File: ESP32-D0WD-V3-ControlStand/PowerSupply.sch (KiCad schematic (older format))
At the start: 5 parts

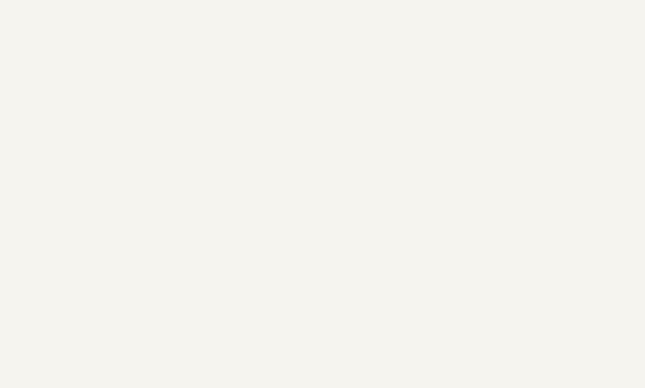
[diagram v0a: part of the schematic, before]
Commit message: Nearly complete schematic.  Added Antenna footprint.
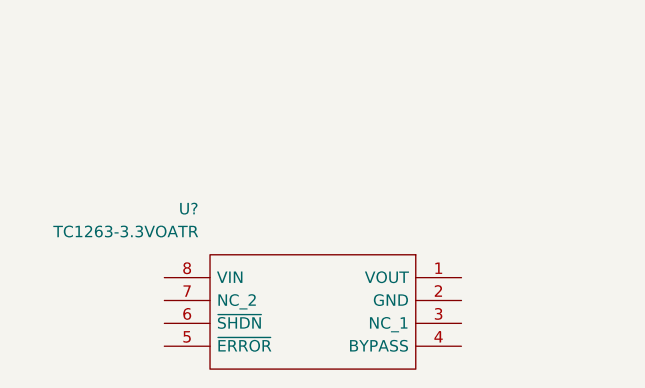
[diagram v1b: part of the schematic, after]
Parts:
- added U?: TC1263-3.3VOATR, Housings_SOIC:SO-8_5.3x6.2mm_Pitch1.27mm, symbol TC1263-3.3VOATR
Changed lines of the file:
@@
 $Descr E 44000 34000
 encoding utf-8
-Sheet 5 6
+Sheet 5 7
 Title "ESP32-D0WD-V3-ControlStand"
 Date "2022-07-25"
@@
 	1    0    0    -1
 $EndComp
+$Comp
+L TC1263-3.3VOATR U?
+U 1 1 62E1190F
+P 5500 4800
+F 0 "U?" H 6650 5100 50  0000 L CNN
+F 1 "TC1263-3.3VOATR" H 6650 5000 50  0000 L CNN
+F 2 "Housings_SOIC:SO-8_5.3x6.2mm_Pitch1.27mm" H 6650 4900 50  0001 L CNN
+F 3 "http://ww1.microchip.com/downloads/en/DeviceDoc/21374D.pdf" H 6650 4800 50  0001 L CNN
+F 4 "LDO Voltage Regulators 500mA Fixed Out Adj" H 6650 4700 50  0001 L CNN "Description"
+F 5 "1.75" H 6650 4600 50  0001 L CNN "Height"
+F 6 "Microchip" H 6650 4300 50  0001 L CNN "Manufacturer_Name"
+F 7 "TC1263-3.3VOATR" H 6650 4200 50  0001 L CNN "Manufacturer_Part_Number"
+	1    5500 4800
+	-1   0    0    -1
+$EndComp
 Wire Wire Line

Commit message: Complete PS, work on parts spec.
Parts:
- added C?: 10uf, Capacitors_SMD:CP_Elec_4x5.7, symbol CP1_Small
- added C? (x2): 4.7uf, Capacitors_SMD:CP_Elec_4x5.7, symbol CP1_Small
- added C?: .1uf, symbol C_Small
- added C?: 1uf, symbol CP1_Small
- added C?: 470pf, symbol C_Small
- added D? (x2): DFLS240-7, Diodes_SMD:D_PowerDI-123, symbol D_Schottky
- added D?: DFLS240-7, Diodes_SMD:D_PowerDI-12, symbol D_Schottky
- added D? (x3): LED, LEDs:LED_0402, symbol LED
- added D?: SMAJ5.0A/TR13, Diodes_SMD:D_SMA, symbol D_Zener_Small_ALT
- added J?: Barrel_Jack, Connectors:BARREL_JACK, symbol Barrel_Jack
- added J?: Battery, Connectors_JST:JST_PH_S2B-PH-SM4-TB_02x2.00mm_Angled, symbol Conn_01x02
- added R?: 330K, Resistors_SMD:R_0402, symbol R
- added R?: 110K, Resistors_SMD:R_0402, symbol R
- added R? (x3): 470, Resistors_SMD:R_0402, symbol R
- added R? (x2): 10K, Resistors_SMD:R_0402, symbol R
- added R?: 2K, Resistors_SMD:R_0402, symbol R
- added R?: 5K, Resistors_SMD:R_0402, symbol R
- added SW?: On/Off, Buttons_Switches_SMD:SW_SPDT_CK-JS102011SAQN, symbol SW_SPDT
- added U?: MCP73871, Housings_DFN_QFN:QFN-20-1EP_4x4mm_Pitch0.5mm, symbol MCP73871
- C?: footprint ~ -> Capacitors_SMD:CP_Elec_8x10; Mouser Part Number 140-REA220M2ABK0811P -> 647-UUX2A220MNL6GS
- C?: footprint ~ -> Capacitors_SMD:CP_Elec_8x10; Mouser Part Number 140-REA221M1EBK0811P -> 647-UWT1E221MNL1GS
- D?: footprint ~ -> Diodes_SMD:D_SMB; Mouser Part Number 625-SB160-E3 -> 610-CMSH1-60TR13
- L?: footprint ~ -> SRN1060:SRN1060; Mouser Part Number PE-52627NL -> 652-SRN1060-331M
- U?: value LM2574N-5.0 -> LM2574HVM-5.0; footprint ~ -> SOIC_Wide:SOIC-14_7.4x8.7mm_Pitch1.27mm; symbol LM2574N-5.0 -> LM2574HVM-5.0; Mouser Part Number 926-LM2574N-5.0/NOPB -> 926-LM2574HVM5.0NOPB
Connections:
- net +12V: now also U?.10 (Vin); no longer U?.5 (Vin)
- net +5V: now also U?.3 (FB), D?.2 (A); no longer U?.1 (FB)
- net GND: now also U?.2 (GND), U?.5 (Oh/Off), U?.6 (PwrGnd), C?.1, C?.2, C?.2, C?.2, C?.2, C?.2, D?.2 (A), J?.2, J?.2 (Pin_2), R?.2, R?.2, R?.2, R?.2, U?.10 (GND), U?.11 (GND), U?.21 (GND); no longer U?.2 (SigGnd), U?.3 (Oh/Off)
- net at D?.2 (K), L?.2: now also U?.12 (Out); no longer U?.7 (Out)
- net +3V3: now reaches U?.1 (VOUT)
- net +3V3: now also C?.1
- net at U?.4 (BYPASS): now also C?.1
- net at U?.6 (~SHDN): now also U?.8 (VIN), C?.2, D?.1 (K), D?.1 (K), SW?.2 (B)
- new net: C?.1, D?.1 (K), D?.2 (A), D?.2 (A), D?.2 (A), J?.1, R?.2, R?.2, U?.18 (IN), U?.19 (IN)
- new net: C?.1, J?.1 (Pin_1), U?.14 (BAT+), U?.15 (BAT+), U?.16 (BAT+)
- new net: C?.1, D?.2 (A), U?.1 (OUT), U?.20 (OUT)
- new net: R?.1, U?.12 (PROG3)
- new net: R?.1, U?.13 (PROG1)
- new net: R?.1, U?.17 (CE), U?.3 (SEL), U?.4 (PROG2), U?.9 (~TE)
- new net: R?.1, R?.1, U?.2 (VPCC)
- new net: R?.1, U?.5 (THERM)
- new net: R?.1, U?.6 (~PG)
- new net: R?.1, U?.7 (STAT2)
- new net: R?.1, U?.8 (STAT1/~LBO)
- new net: D?.1 (K), R?.2 (x3)
- new net: D?.1 (K), SW?.1 (A)
- new net VBUS: D?.2 (A)
- no-connect marks 0 -> 4
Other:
- moved on the sheet: U?

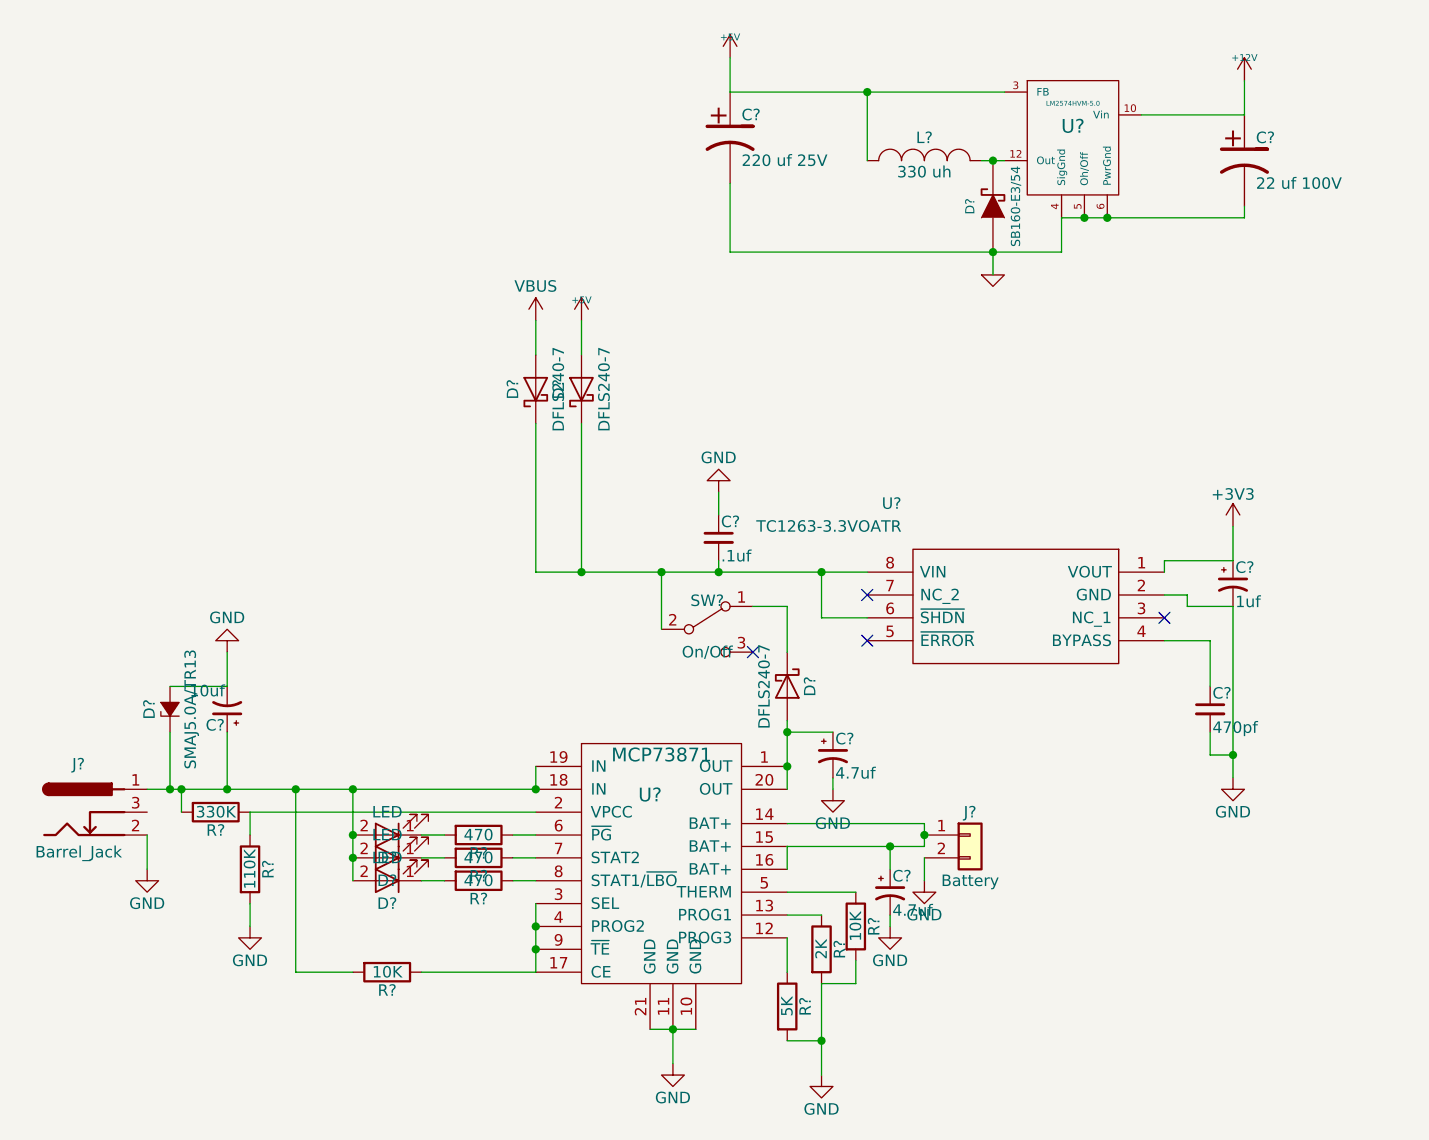
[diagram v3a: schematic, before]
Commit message: Completed parts spec for ESP32-D0WD-V3-ControlStand.
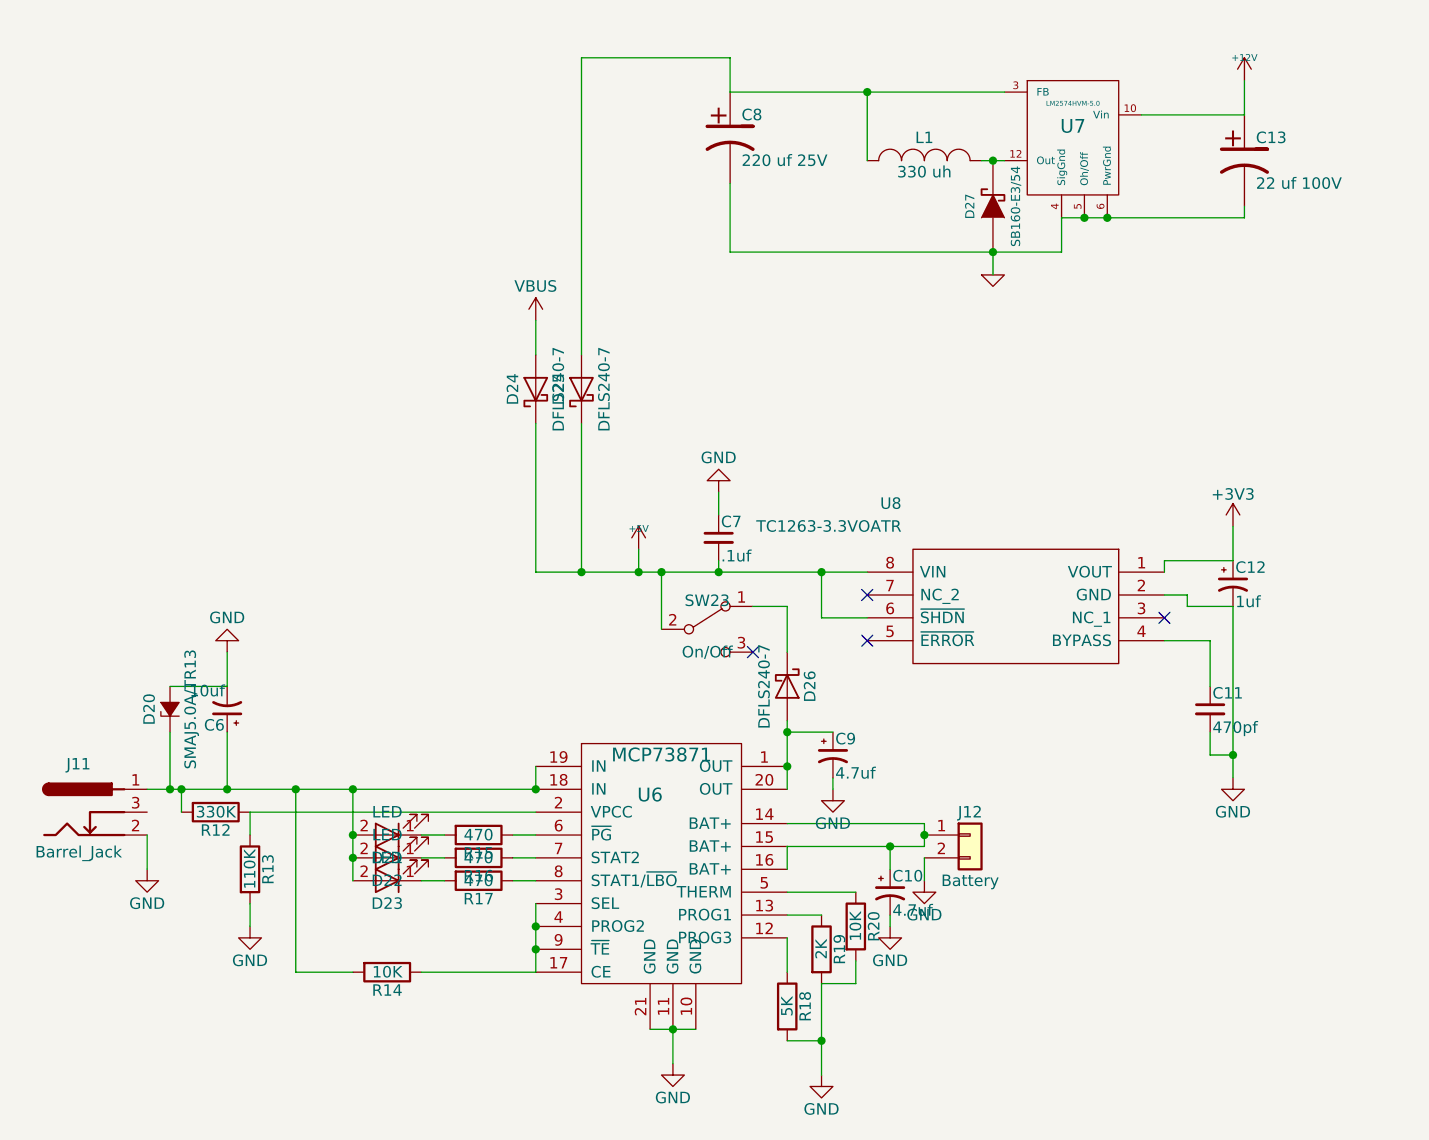
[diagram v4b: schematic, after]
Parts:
- C11: renamed from C?; footprint (none) -> Capacitors_SMD:C_0402; Mouser Part Number (none) -> 80-C0402C471K4RAUTO
- C12: renamed from C?; footprint (none) -> MyCaps:C_0603_POL; Mouser Part Number (none) -> 74-TMCJ1C105MTRF
- C7: renamed from C?; footprint (none) -> Capacitors_SMD:C_0402; Mouser Part Number (none) -> 81-GRM155R62A104KE4J
- gave numbers to parts that had none: 29
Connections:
- net +5V: now also C7.2, D24.1 (K), D25.1 (K), SW23.2 (B), U8.6 (~SHDN), U8.8 (VIN); no longer C8.1, D25.2 (A), L1.1, U7.3 (FB)
- new net: C8.1, D25.2 (A), L1.1, U7.3 (FB)

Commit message: Working on the PCB Layout.
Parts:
- D25: footprint Diodes_SMD:D_PowerDI-12 -> Diodes_SMD:D_PowerDI-123
- J12: footprint Connectors_JST:JST_PH_S2B-PH-SM4-TB_02x2.00mm_Angled -> Connectors_JST:JST_PH_B2B-PH-SM4-TB_02x2.00mm_Straight; Manufacturer_Part_Number (none) -> B2B-PH-SM4-TB; Manufaturer_Name (none) -> JST
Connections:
- net +3V3 renamed +3.3V
- no-connect marks 4 -> 13
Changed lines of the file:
@@
 LIBS:mcp73871
 LIBS:lm2574n-5
+LIBS:mechanical
+LIBS:graphic_symbols
 LIBS:ESP32-D0WD-V3-ControlStand-cache
 EELAYER 25 0
@@
 $EndComp
 $Comp
-L GND-RESCUE-ESP32ControlStand #PWR56
+L GND-RESCUE-ESP32ControlStand #PWR045
 U 1 1 62DF1557
 P 4850 3400
-F 0 "#PWR56" H 4850 3400 30  0001 C CNN
+F 0 "#PWR045" H 4850 3400 30  0001 C CNN
 F 1 "GND" H 4850 3330 30  0001 C CNN
 F 2 "" H 4850 3400 60  0000 C CNN
@@
 $EndComp
 $Comp
-L +12V #PWR59
+L +12V #PWR046
 U 1 1 62DF1558
 P 5950 2550
-F 0 "#PWR59" H 5950 2500 20  0001 C CNN
+F 0 "#PWR046" H 5950 2500 20  0001 C CNN
 F 1 "+12V" H 5950 2650 30  0000 C CNN
 F 2 "" H 5950 2550 60  0000 C CNN
@@
 $EndComp
 $Comp
-L VBUS #PWR48
+L VBUS #PWR047
 U 1 1 62E2AE4F
 P 2850 3600
-F 0 "#PWR48" H 2850 3450 50  0001 C CNN
+F 0 "#PWR047" H 2850 3450 50  0001 C CNN
 F 1 "VBUS" H 2850 3750 50  0000 C CNN
 F 2 "" H 2850 3600 50  0001 C CNN
@@
 $EndComp
 $Comp
-L +5V #PWR49
+L +5V #PWR048
 U 1 1 62E2AF43
 P 3300 4600
-F 0 "#PWR49" H 3300 4690 20  0001 C CNN
+F 0 "#PWR048" H 3300 4690 20  0001 C CNN
 F 1 "+5V" H 3300 4690 30  0000 C CNN
 F 2 "" H 3300 4600 60  0000 C CNN
@@
 $EndComp
 $Comp
-L GND #PWR45
+L GND #PWR049
 U 1 1 62E2B93A
 P 1150 6000
-F 0 "#PWR45" H 1150 5750 50  0001 C CNN
+F 0 "#PWR049" H 1150 5750 50  0001 C CNN
 F 1 "GND" H 1150 5850 50  0000 C CNN
 F 2 "" H 1150 6000 50  0001 C CNN
@@
 F 0 "D25" H 3050 4000 50  0000 C CNN
 F 1 "DFLS240-7" H 3050 3800 50  0000 C CNN
-F 2 "Diodes_SMD:D_PowerDI-12" H 3050 3900 50  0001 C CNN
+F 2 "Diodes_SMD:D_PowerDI-123" H 3050 3900 50  0001 C CNN
 F 3 "" H 3050 3900 50  0001 C CNN
 F 4 "621-DFLS240-7" H 3050 3900 60  0001 C CNN "Mouser Part Number"
@@
 F 0 "J12" H 4750 5950 50  0000 C CNN
 F 1 "Battery" H 4750 5650 50  0000 C CNN
-F 2 "Connectors_JST:JST_PH_S2B-PH-SM4-TB_02x2.00mm_Angled" H 4750 5850 50  0001 C CNN
+F 2 "Connectors_JST:JST_PH_B2B-PH-SM4-TB_02x2.00mm_Straight" H 4750 5850 50  0001 C CNN
 F 3 "" H 4750 5850 50  0001 C CNN
+F 4 "JST" H 4750 5850 60  0001 C CNN "Manufaturer_Name"
+F 5 "B2B-PH-SM4-TB" H 4750 5850 60  0001 C CNN "Manufacturer_Part_Number"
 	1    4750 5850
 	1    0    0    -1
 $EndComp
 $Comp
-L GND #PWR55
+L GND #PWR050
 U 1 1 62E2DC33
 P 4550 6050
-F 0 "#PWR55" H 4550 5800 50  0001 C CNN
+F 0 "#PWR050" H 4550 5800 50  0001 C CNN
 F 1 "GND" H 4550 5900 50  0000 C CNN
 F 2 "" H 4550 6050 50  0001 C CNN
@@
 Connection ~ 3450 6700
 $Comp
-L GND #PWR50
+L GND #PWR051
 U 1 1 62E30901
 P 3450 6850
-F 0 "#PWR50" H 3450 6600 50  0001 C CNN
+F 0 "#PWR051" H 3450 6600 50  0001 C CNN
 F 1 "GND" H 3450 6700 50  0000 C CNN
 F 2 "" H 3450 6850 50  0001 C CNN
@@
 	1600 5750 1600 5850
 $Comp
-L GND #PWR47
+L GND #PWR052
 U 1 1 62E319CD
 P 1600 6250
-F 0 "#PWR47" H 1600 6000 50  0001 C CNN
+F 0 "#PWR052" H 1600 6000 50  0001 C CNN
 F 1 "GND" H 1600 6100 50  0000 C CNN
 F 2 "" H 1600 6250 50  0001 C CNN
@@
 	1250 5200 1500 5200
 $Comp
-L GND #PWR46
+L GND #PWR053
 U 1 1 62E3313D
 P 1500 5050
-F 0 "#PWR46" H 1500 4800 50  0001 C CNN
+F 0 "#PWR053" H 1500 4800 50  0001 C CNN
 F 1 "GND" H 1500 4900 50  0000 C CNN
 F 2 "" H 1500 5050 50  0001 C CNN
@@
 Connection ~ 3950 5400
 $Comp
-L GND #PWR53
+L GND #PWR054
 U 1 1 62E341D5
 P 4150 5650
-F 0 "#PWR53" H 4150 5400 50  0001 C CNN
+F 0 "#PWR054" H 4150 5400 50  0001 C CNN
 F 1 "GND" H 4150 5500 50  0000 C CNN
 F 2 "" H 4150 5650 50  0001 C CNN
@@
 	4150 5600 4150 5650
 $Comp
-L GND #PWR54
+L GND #PWR055
 U 1 1 62E342FA
 P 4400 6250
-F 0 "#PWR54" H 4400 6000 50  0001 C CNN
+F 0 "#PWR055" H 4400 6000 50  0001 C CNN
 F 1 "GND" H 4400 6100 50  0000 C CNN
 F 2 "" H 4400 6250 50  0001 C CNN
@@
 	4250 6500 4250 6400
 $Comp
-L GND #PWR52
+L GND #PWR056
 U 1 1 62E35319
 P 4100 6900
-F 0 "#PWR52" H 4100 6650 50  0001 C CNN
+F 0 "#PWR056" H 4100 6650 50  0001 C CNN
 F 1 "GND" H 4100 6750 50  0000 C CNN
 F 2 "" H 4100 6900 50  0001 C CNN
@@
 Connection ~ 3650 4700
 $Comp
-L GND #PWR51
+L GND #PWR057
 U 1 1 62E36914
 P 3650 4350
-F 0 "#PWR51" H 3650 4100 50  0001 C CNN
+F 0 "#PWR057" H 3650 4100 50  0001 C CNN
 F 1 "GND" H 3650 4200 50  0000 C CNN
 F 2 "" H 3650 4350 50  0001 C CNN
@@
 	5800 5500 5800 5400
 $Comp
-L GND #PWR58
+L GND #PWR058
 U 1 1 62E37013
 P 5900 5600
-F 0 "#PWR58" H 5900 5350 50  0001 C CNN
+F 0 "#PWR058" H 5900 5350 50  0001 C CNN
 F 1 "GND" H 5900 5450 50  0000 C CNN
 F 2 "" H 5900 5600 50  0001 C CNN
@@
 Connection ~ 5900 5500
 $Comp
-L +3V3 #PWR57
+L +3.3V-RESCUE-ESP32ControlStand #PWR059
 U 1 1 62E370EF
 P 5900 4500
-F 0 "#PWR57" H 5900 4350 50  0001 C CNN
-F 1 "+3V3" H 5900 4640 50  0000 C CNN
+F 0 "#PWR059" H 5900 4350 50  0001 C CNN
+F 1 "+3.3V-RESCUE-ESP32ControlStand" H 5900 4640 50  0000 C CNN
 F 2 "" H 5900 4500 50  0001 C CNN
 F 3 "" H 5900 4500 50  0001 C CNN
@@
 	3300 4600 3300 4700
 Connection ~ 3300 4700
+NoConn ~ 5500 2800
+NoConn ~ 5500 2900
+NoConn ~ 5100 2450
+NoConn ~ 5150 2450
+NoConn ~ 5200 2450
+NoConn ~ 5250 2450
+NoConn ~ 5300 2450
+NoConn ~ 5350 2450
+NoConn ~ 4800 2300
 $EndSCHEMATC

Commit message: Completed V0.0 PCB.
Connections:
- net +3.3V renamed +3V3
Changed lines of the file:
@@
 $EndComp
 $Comp
-L GND-RESCUE-ESP32ControlStand #PWR045
+L GND #PWR047
 U 1 1 62DF1557
 P 4850 3400
-F 0 "#PWR045" H 4850 3400 30  0001 C CNN
+F 0 "#PWR047" H 4850 3400 30  0001 C CNN
 F 1 "GND" H 4850 3330 30  0001 C CNN
 F 2 "" H 4850 3400 60  0000 C CNN
@@
 $EndComp
 $Comp
-L +12V #PWR046
+L +12V #PWR048
 U 1 1 62DF1558
 P 5950 2550
-F 0 "#PWR046" H 5950 2500 20  0001 C CNN
+F 0 "#PWR048" H 5950 2500 20  0001 C CNN
 F 1 "+12V" H 5950 2650 30  0000 C CNN
 F 2 "" H 5950 2550 60  0000 C CNN
@@
 $EndComp
 $Comp
-L VBUS #PWR047
+L VBUS #PWR049
 U 1 1 62E2AE4F
 P 2850 3600
-F 0 "#PWR047" H 2850 3450 50  0001 C CNN
+F 0 "#PWR049" H 2850 3450 50  0001 C CNN
 F 1 "VBUS" H 2850 3750 50  0000 C CNN
 F 2 "" H 2850 3600 50  0001 C CNN
@@
 $EndComp
 $Comp
-L +5V #PWR048
+L +5V #PWR050
 U 1 1 62E2AF43
 P 3300 4600
-F 0 "#PWR048" H 3300 4690 20  0001 C CNN
+F 0 "#PWR050" H 3300 4690 20  0001 C CNN
 F 1 "+5V" H 3300 4690 30  0000 C CNN
 F 2 "" H 3300 4600 60  0000 C CNN
@@
 $EndComp
 $Comp
-L GND #PWR049
+L GND #PWR051
 U 1 1 62E2B93A
 P 1150 6000
-F 0 "#PWR049" H 1150 5750 50  0001 C CNN
+F 0 "#PWR051" H 1150 5750 50  0001 C CNN
 F 1 "GND" H 1150 5850 50  0000 C CNN
 F 2 "" H 1150 6000 50  0001 C CNN
@@
 $EndComp
 $Comp
-L GND #PWR050
+L GND #PWR052
 U 1 1 62E2DC33
 P 4550 6050
-F 0 "#PWR050" H 4550 5800 50  0001 C CNN
+F 0 "#PWR052" H 4550 5800 50  0001 C CNN
 F 1 "GND" H 4550 5900 50  0000 C CNN
 F 2 "" H 4550 6050 50  0001 C CNN
@@
 Connection ~ 3450 6700
 $Comp
-L GND #PWR051
+L GND #PWR053
 U 1 1 62E30901
 P 3450 6850
-F 0 "#PWR051" H 3450 6600 50  0001 C CNN
+F 0 "#PWR053" H 3450 6600 50  0001 C CNN
 F 1 "GND" H 3450 6700 50  0000 C CNN
 F 2 "" H 3450 6850 50  0001 C CNN
@@
 	1600 5750 1600 5850
 $Comp
-L GND #PWR052
+L GND #PWR054
 U 1 1 62E319CD
 P 1600 6250
-F 0 "#PWR052" H 1600 6000 50  0001 C CNN
+F 0 "#PWR054" H 1600 6000 50  0001 C CNN
 F 1 "GND" H 1600 6100 50  0000 C CNN
 F 2 "" H 1600 6250 50  0001 C CNN
@@
 	1250 5200 1500 5200
 $Comp
-L GND #PWR053
+L GND #PWR055
 U 1 1 62E3313D
 P 1500 5050
-F 0 "#PWR053" H 1500 4800 50  0001 C CNN
+F 0 "#PWR055" H 1500 4800 50  0001 C CNN
 F 1 "GND" H 1500 4900 50  0000 C CNN
 F 2 "" H 1500 5050 50  0001 C CNN
@@
 Connection ~ 3950 5400
 $Comp
-L GND #PWR054
+L GND #PWR056
 U 1 1 62E341D5
 P 4150 5650
-F 0 "#PWR054" H 4150 5400 50  0001 C CNN
+F 0 "#PWR056" H 4150 5400 50  0001 C CNN
 F 1 "GND" H 4150 5500 50  0000 C CNN
 F 2 "" H 4150 5650 50  0001 C CNN
@@
 	4150 5600 4150 5650
 $Comp
-L GND #PWR055
+L GND #PWR057
 U 1 1 62E342FA
 P 4400 6250
-F 0 "#PWR055" H 4400 6000 50  0001 C CNN
+F 0 "#PWR057" H 4400 6000 50  0001 C CNN
 F 1 "GND" H 4400 6100 50  0000 C CNN
 F 2 "" H 4400 6250 50  0001 C CNN
@@
 	4250 6500 4250 6400
 $Comp
-L GND #PWR056
+L GND #PWR058
 U 1 1 62E35319
 P 4100 6900
-F 0 "#PWR056" H 4100 6650 50  0001 C CNN
+F 0 "#PWR058" H 4100 6650 50  0001 C CNN
 F 1 "GND" H 4100 6750 50  0000 C CNN
 F 2 "" H 4100 6900 50  0001 C CNN
@@
 Connection ~ 3650 4700
 $Comp
-L GND #PWR057
+L GND #PWR059
 U 1 1 62E36914
 P 3650 4350
-F 0 "#PWR057" H 3650 4100 50  0001 C CNN
+F 0 "#PWR059" H 3650 4100 50  0001 C CNN
 F 1 "GND" H 3650 4200 50  0000 C CNN
 F 2 "" H 3650 4350 50  0001 C CNN
@@
 	5800 5500 5800 5400
 $Comp
-L GND #PWR058
+L GND #PWR060
 U 1 1 62E37013
 P 5900 5600
-F 0 "#PWR058" H 5900 5350 50  0001 C CNN
+F 0 "#PWR060" H 5900 5350 50  0001 C CNN
 F 1 "GND" H 5900 5450 50  0000 C CNN
 F 2 "" H 5900 5600 50  0001 C CNN
@@
 Connection ~ 5900 5500
 $Comp
-L +3.3V-RESCUE-ESP32ControlStand #PWR059
+L +3.3V #PWR061
 U 1 1 62E370EF
 P 5900 4500
-F 0 "#PWR059" H 5900 4350 50  0001 C CNN
-F 1 "+3.3V-RESCUE-ESP32ControlStand" H 5900 4640 50  0000 C CNN
+F 0 "#PWR061" H 5900 4350 50  0001 C CNN
+F 1 "+3.3V" H 5900 4640 50  0000 C CNN
 F 2 "" H 5900 4500 50  0001 C CNN
 F 3 "" H 5900 4500 50  0001 C CNN
